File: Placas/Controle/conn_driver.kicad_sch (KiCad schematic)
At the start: 5 parts, among them J12 Conn_02x07_Odd_Even, J13 Conn_01x02_Pin, J14 Conn_01x02_Pin, U11 HEF4093B

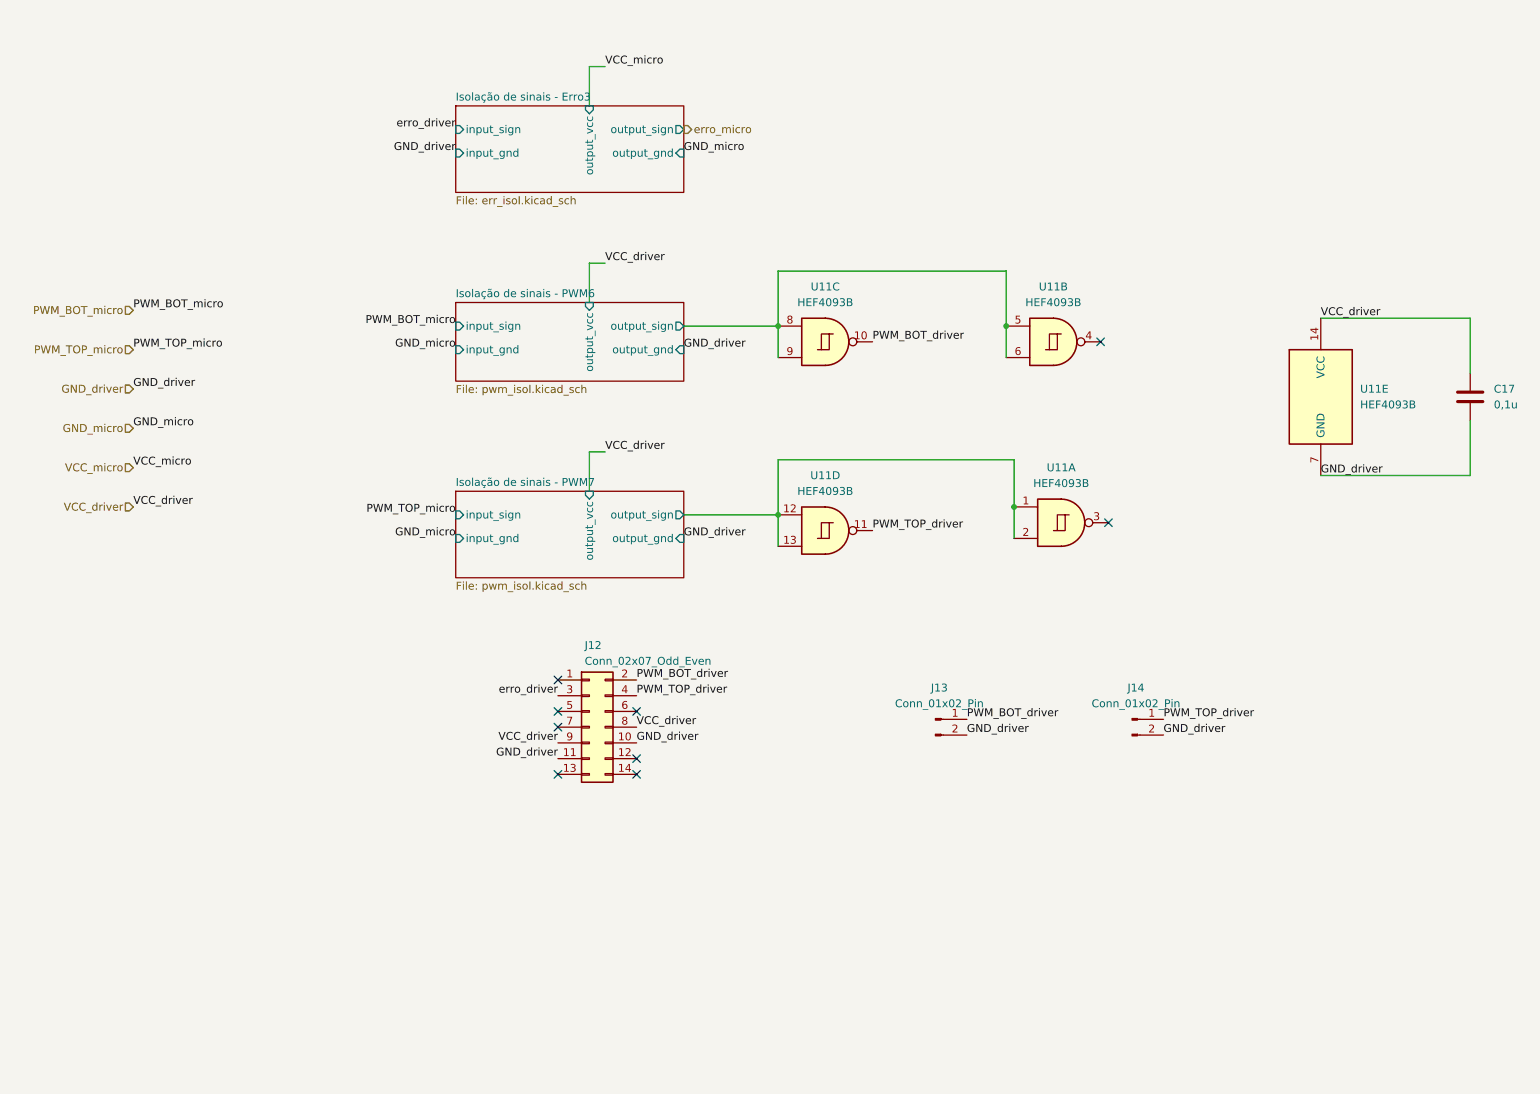
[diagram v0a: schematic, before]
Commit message: Adição de circuitos opcionais para PWM
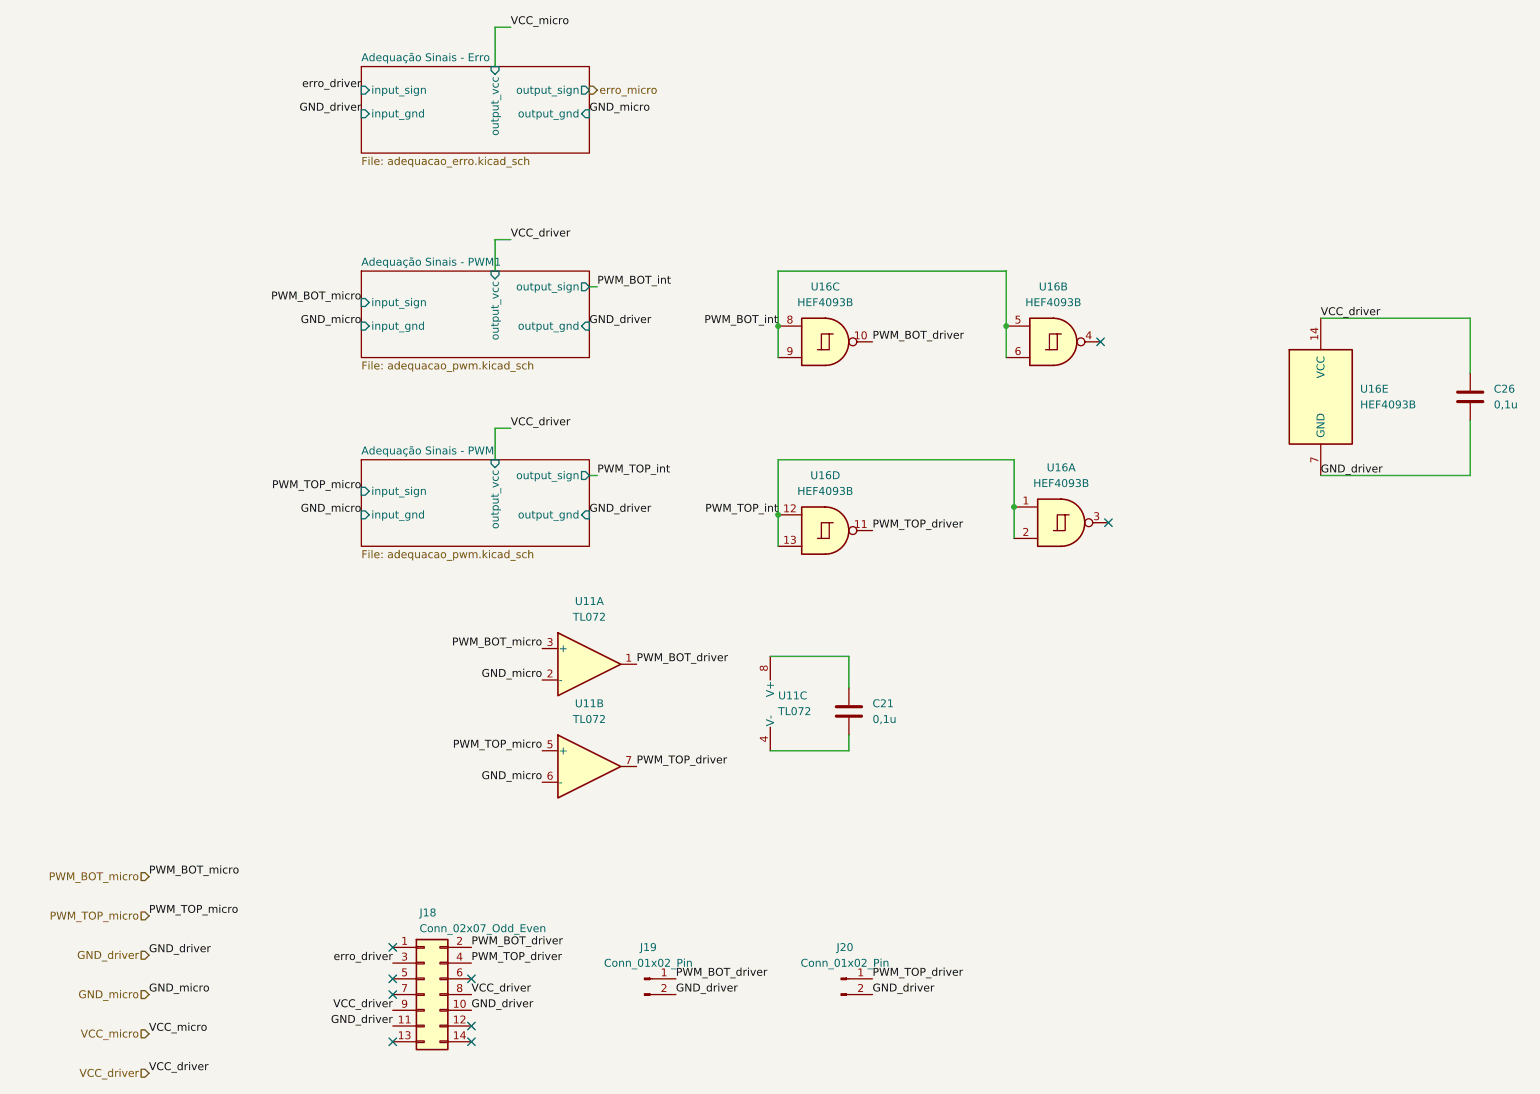
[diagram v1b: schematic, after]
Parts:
- added C21: 0,1u, Capacitor_THT:C_Disc_D8.0mm_W5.0mm_P7.50mm, symbol Device:C
- added U11: TL072, Package_DIP:DIP-8_W7.62mm, symbol Amplifier_Operational:TL072
- renumbered C17 to C26, J12 to J18, J13 to J19, J14 to J20, U11 to U16
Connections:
- net GND_micro: now also U11.2 (-), U11.6 (-)
- net PWM_BOT_driver: now also U11.1
- net PWM_BOT_micro: now also U11.3 (+)
- net PWM_TOP_driver: now also U11.7
- net PWM_TOP_micro: now also U11.5 (+)
- net Isolação de sinais - PWM6/output_sign renamed PWM_BOT_int
- net Isolação de sinais - PWM7/output_sign renamed PWM_TOP_int
- new net: C21.2, U11.4 (V-)
- new net: C21.1, U11.8 (V+)
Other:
- removed sheet Isolação de sinais - Erro3
- removed sheet Isolação de sinais - PWM6
- removed sheet Isolação de sinais - PWM7
- added sheet Adequação Sinais - Erro (adequacao_erro.kicad_sch)
- added sheet Adequação Sinais - PWM (adequacao_pwm.kicad_sch)
- added sheet Adequação Sinais - PWM1 (adequacao_pwm.kicad_sch)
- moved on the sheet: J18, J19, J20

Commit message: Modificações nas duas placas, adição de furos para montagem, melhora na posição dos micros e conectores para comunicação SPI
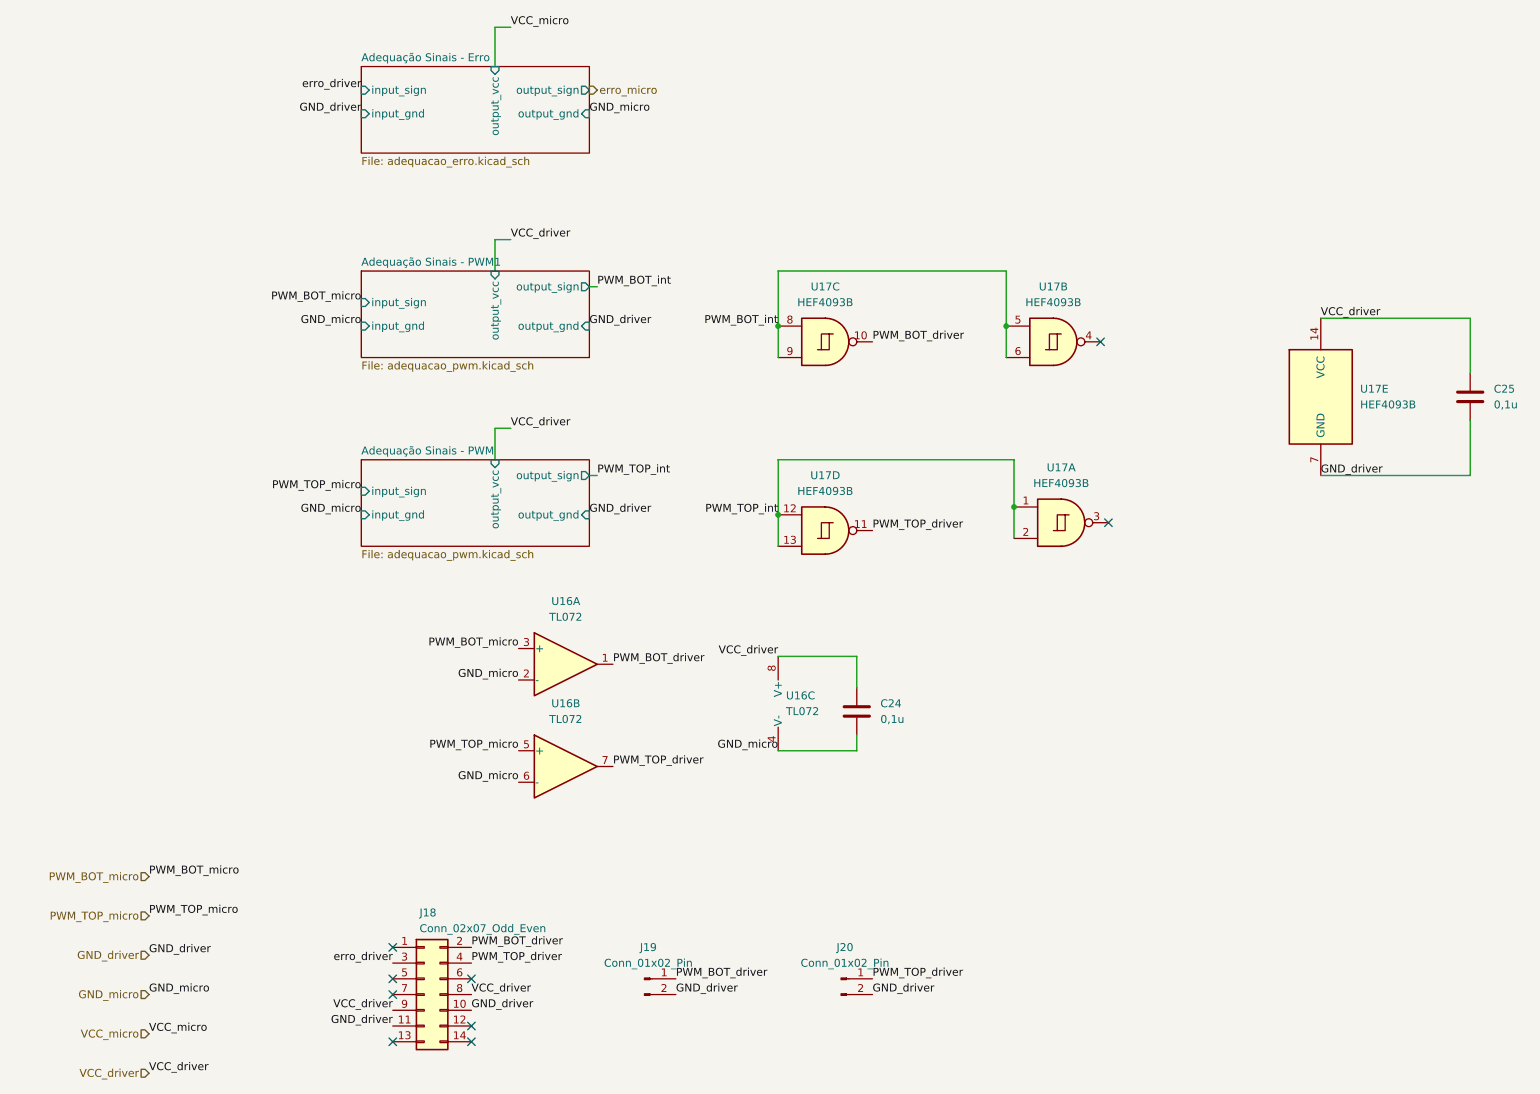
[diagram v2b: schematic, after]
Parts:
- removed U11: TL072, Package_DIP:DIP-8_W7.62mm, symbol Amplifier_Operational:TL072
- added U16: TL072, Package_DIP:DIP-8_W7.62mm, symbol Amplifier_Operational:TL072
- C24: renamed from C21; footprint Capacitor_THT:C_Disc_D8.0mm_W5.0mm_P7.50mm -> Capacitor_SMD:C_0805_2012Metric_Pad1.18x1.45mm_HandSolder
- C25: renamed from C26; footprint Capacitor_THT:C_Disc_D8.0mm_W5.0mm_P7.50mm -> Capacitor_SMD:C_0805_2012Metric_Pad1.18x1.45mm_HandSolder
- J18: footprint Connector_IDC:IDC-Header_2x07_P2.54mm_Latch_Vertical -> IDC Connectors:IDC_Header_2x07
- renumbered U16 to U17
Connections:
- net GND_micro: now also C24.2, U16.2 (-), U16.4 (V-), U16.6 (-)
- net PWM_BOT_driver: now also U16.1
- net PWM_BOT_micro: now also U16.3 (+)
- net PWM_TOP_driver: now also U16.7
- net PWM_TOP_micro: now also U16.5 (+)
- net VCC_driver: now also C24.1, U16.8 (V+)
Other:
- moved on the sheet: C24
